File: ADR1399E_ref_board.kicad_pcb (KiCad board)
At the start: 4 copper layers, 119 x 60 mm, 103 parts, among them IC1 ADP7142ARDZ-R7, J1 Conn_01x02_Pin, J2 USB_C_Receptacle_PowerOnly_6P, J3 Conn_Coaxial, J4 S4B-XH-A, P1 JST_B2P_VH, Q1 MMBT3906, Q2 2N7002, U2 TPS61085DGK, U3 OPA182IDR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

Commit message: moved VH connector to center
avoid collision with Banana sockets (in case)
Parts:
- moved D2 26.3 mm to (138.4, 111.1), turned to -90 degrees
- moved P1 15.7 mm to (137.2, 104.0)
- moved R25 9.06 mm to (127.6, 104.2)
- moved R21 7.30 mm to (134.7, 109.6)
- moved TP8 6.22 mm to (143.5, 112.5)
- moved R18 5.10 mm to (131.4, 99.4), turned to -90 degrees
- moved C17 3.00 mm to (124.6, 94.9)
- moved C18 3.00 mm to (124.6, 92.6)
- moved TP7 2.69 mm to (143.5, 95.4)
- moved TP6 2.50 mm to (44.0, 128.0)
- moved U4 2.34 mm to (125.2, 99.0)
- moved RN1 1.10 mm to (122.0, 111.4)
- moved C23 0.90 mm to (122.1, 104.4)
- moved U7 0.89 mm to (121.9, 118.6)
- moved JP11 0.60 mm to (121.8, 125.8)
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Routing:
- net Net-(RN1-R1.2): track 16.3 -> 6.47 mm
- net /10V_Out: track 45.4 -> 40.1 mm
- net GND: track 42.0 -> 38.4 mm, vias 319 -> 324
- net Net-(U3-OUT): track 12.3 -> 9.95 mm
- net Net-(JP11-B): track 24.8 -> 26.7 mm
- net Net-(JP9-A): track 6.21 -> 7.31 mm
- net +BATT: track 96.1 -> 95.0 mm
- net Net-(Q1-B): track 36.9 -> 37.8 mm
- net Net-(RN1-R1.1): track 18.0 -> 17.2 mm
- net Net-(U4--IN): track 10.9 -> 10.3 mm
- net /15V_Out: track 42.2 -> 41.6 mm
- net Net-(JP8-A): track 4.98 -> 5.51 mm

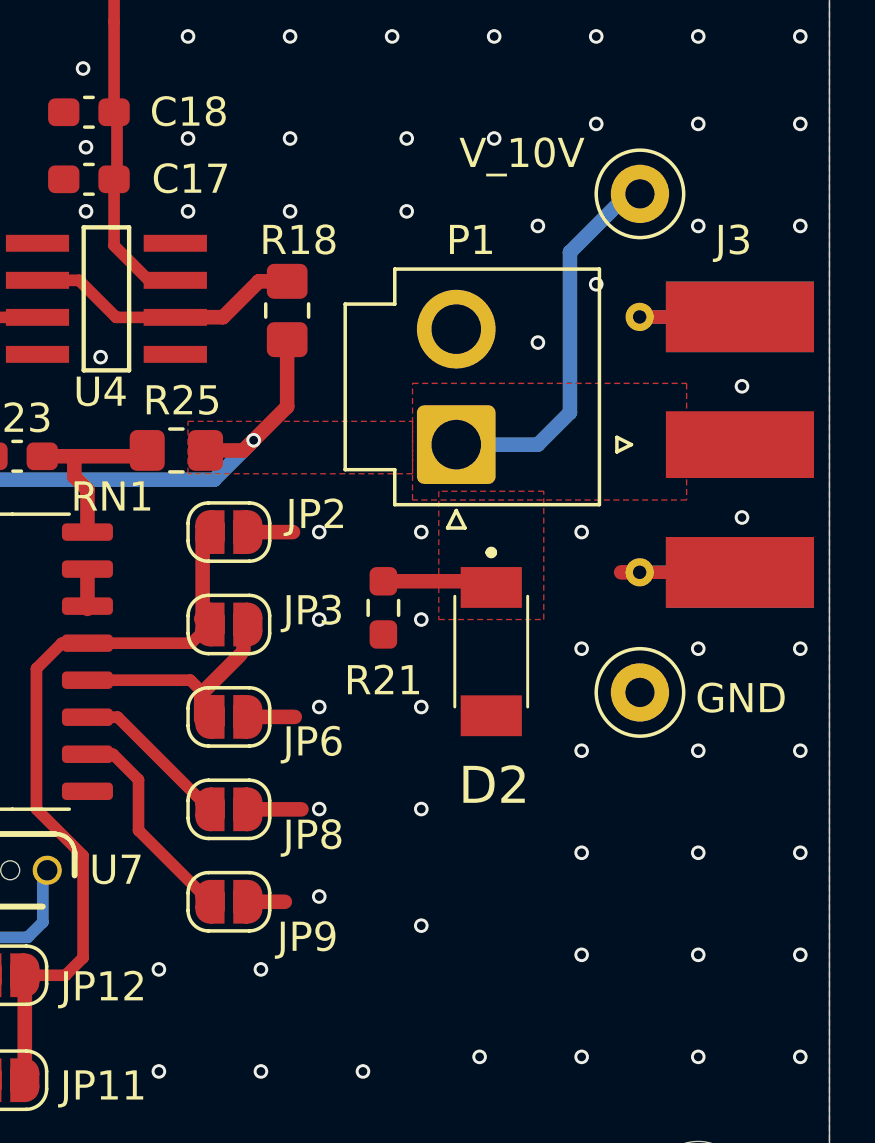
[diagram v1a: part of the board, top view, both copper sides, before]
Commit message: really centered the VH connector
And added VH housing 3d model
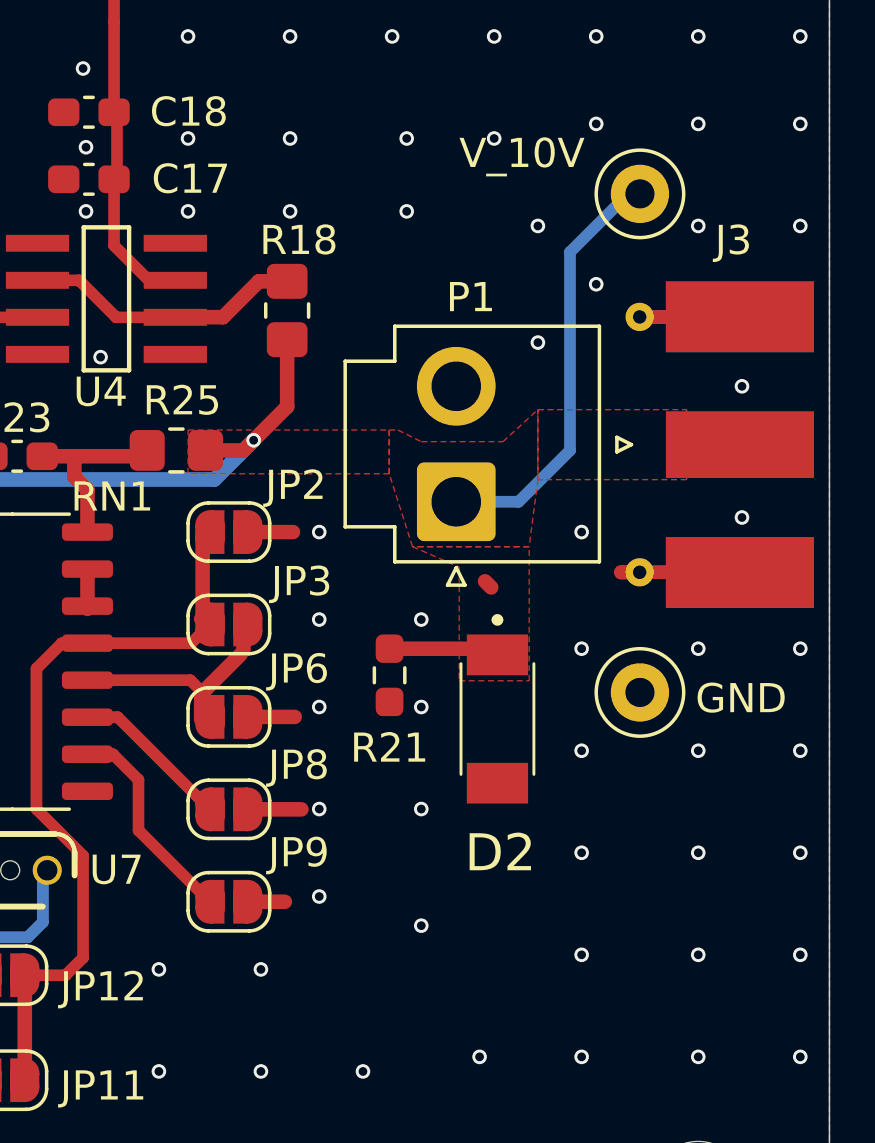
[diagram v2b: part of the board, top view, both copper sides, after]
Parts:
- moved D2 2.32 mm to (138.6, 113.4)
- moved R21 2.32 mm to (134.9, 111.9)
- moved P1 1.96 mm to (137.2, 106.0)
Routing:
- net /10V_Out: track 40.1 -> 41.7 mm
- net GND: vias 324 -> 323
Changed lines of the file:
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@@
 	(footprint "Resistor_SMD:R_0603_1608Metric_Pad0.98x0.95mm_HandSolder"
 		(layer "F.Cu")
-		(at 134.7 109.6 -90)
+		(at 134.9125 111.9125 -90)
 		(descr "Resistor SMD 0603 (1608 Metric), square (rectangular) end terminal, IPC-7351 nominal with elongated pad for handsoldering. (Body size source: IPC-SM-782 page 72, https://www.pcb-3d.com/wordpress/wp-content/uploads/ipc-sm-782a_amendment_1_and_2.pdf), generated with kicad-footprint-generator")
 		(tags "resistor handsolder")
@@
 		(tags "solder jumper open")
 		(property "Reference" "JP8"
-			(at 2.9 0.89 0)
+			(at 2.4 -1.51 0)
 			(layer "F.SilkS")
 			(effects
@@
 		(tags "solder jumper open")
 		(property "Reference" "JP9"
-			(at 2.7 1.22 0)
+			(at 2.4 -1.68 0)
 			(layer "F.SilkS")
 			(effects
@@
 		(tags "solder jumper open")
 		(property "Reference" "JP2"
-			(at 3 -0.6 0)
+			(at 2.3 -1.6 0)
 			(layer "F.SilkS")
 			(effects
@@
 	(footprint "Connector_JST:JST_VH_B2P-VH_1x02_P3.96mm_Vertical"
 		(layer "F.Cu")
-		(at 137.2 104 90)
+		(at 137.2 105.96 90)
 		(descr "JST VH series connector, B2P-VH (http://www.jst-mfg.com/product/pdf/eng/eVH.pdf), generated with kicad-footprint-generator")
 		(tags "connector JST VH vertical")
@@
 			)
 		)
+		(model "${KICAD_3RD_PARTY}/3dmodels/VHR-2N.STEP"
+			(offset
+				(xyz 2 0 17)
+			)
+			(scale
+				(xyz 1 1 1)
+			)
+			(rotate
+				(xyz 90 -0 -0)
+			)
+		)
 	)
 	(footprint "Capacitor_SMD:C_0603_1608Metric_Pad1.08x0.95mm_HandSolder"
@@
 		(tags "solder jumper open")
 		(property "Reference" "JP6"
-			(at 2.9 0.86 0)
+			(at 2.4 -1.64 0)
 			(layer "F.SilkS")
 			(effects
@@
 		(tags "solder jumper open")
 		(property "Reference" "JP3"
-			(at 2.9 -0.47 0)
+			(at 2.5 -1.47 0)
 			(layer "F.SilkS")
 			(effects
@@
 	(footprint "Samacsys:PMEG3050EP115"
 		(layer "F.Cu")
-		(at 138.4 111.1 -90)
+		(at 138.6125 113.4125 -90)
 		(descr "SOD128")
 		(tags "Diode ESD (Uni-directional)")
@@
 	)
 	(via
-		(at 136 107)
-		(size 0.5)
-		(drill 0.3)
-		(layers "F.Cu" "B.Cu")
-		(free yes)
-		(net 1)
-	)
-	(via
 		(at 93.1 98.4)
 		(size 0.5)
@@
 	)
 	(segment
-		(start 134.7 108.6875)
-		(end 138.1875 108.6875)
+		(start 134.9125 111)
+		(end 138.4 111)
 		(width 0.5)
 		(layer "F.Cu")
@@
 	)
 	(segment
-		(start 141.1 102.9)
-		(end 140 104)
+		(start 130.25 103.85)
+		(end 128.9 105.2)
 		(width 0.5)
 		(layer "B.Cu")
@@
 	)
 	(segment
-		(start 141.1 97.4)
-		(end 141.1 98)
-		(width 0.5)
+		(start 139.34 105.96)
+		(end 137.2 105.96)
+		(width 0.4)
 		(layer "B.Cu")
 		(net 20)
 	)
 	(segment
-		(start 130.25 103.85)
-		(end 128.9 105.2)
-		(width 0.5)
+		(start 141.1 97.4)
+		(end 141.1 104.2)
+		(width 0.4)
 		(layer "B.Cu")
 		(net 20)
 	)
 	(segment
-		(start 141.1 98)
-		(end 141.1 102.9)
-		(width 0.5)
+		(start 141.1 104.2)
+		(end 139.34 105.96)
+		(width 0.4)
 		(layer "B.Cu")
 		(net 20)
@@
 		(start 143.5 95)
 		(end 141.1 97.4)
-		(width 0.5)
-		(layer "B.Cu")
-		(net 20)
-	)
-	(segment
-		(start 140 104)
-		(end 137.2 104)
-		(width 0.5)
+		(width 0.4)
 		(layer "B.Cu")
 		(net 20)
@@
 		(polygon
 			(pts
-				(xy 128 103.2) (xy 135.7 103.2) (xy 135.7 105) (xy 128 105)
+				(xy 128 103.5) (xy 134.9 103.5) (xy 134.9 105) (xy 128 105)
 			)
 		)
@@
 		(polygon
 			(pts
-				(xy 145.1 101.9) (xy 145.1 105.9) (xy 135.7 105.9) (xy 135.7 101.9)
+				(xy 145.1 102.8) (xy 145.1 105.2) (xy 140 105.2) (xy 140 102.8)
 			)
 		)
@@
 	)
 	(zone
+		(net 20)
+		(net_name "/10V_Out")
+		(layer "F.Cu")
+		(hatch edge 0.5)
+		(priority 14)
+		(connect_pads yes
+			(clearance 0.2)
+		)
+		(min_thickness 0.25)
+		(filled_areas_thickness no)
+		(fill yes
+			(thermal_gap 0.5)
+			(thermal_bridge_width 0.5)
+		)
+		(polygon
+			(pts
+				(xy 134.9 103.5) (xy 135.2 103.5) (xy 136 103.9) (xy 138.8 103.9) (xy 140 102.8) (xy 140 105.2)
+				(xy 139.7 107.5) (xy 135.7 107.5) (xy 134.9 105)
+			)
+		)
+	)
+	(zone
 		(net 2)
 		(net_name "+5V")
@@
 		(polygon
 			(pts
-				(xy 136.6 110) (xy 140.2 110) (xy 140.2 105.6) (xy 136.6 105.6)
+				(xy 137.3 108.2) (xy 137.3 112.1) (xy 139.7 112.1) (xy 139.7 107.5) (xy 135.7 107.5)
 			)
 		)

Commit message: Update ADR1399E_ref_board.kicad_pcb
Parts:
- moved P1 0.14 mm to (137.2, 106.1)
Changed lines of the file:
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@@
 	(footprint "Connector_JST:JST_VH_B2P-VH_1x02_P3.96mm_Vertical"
 		(layer "F.Cu")
-		(at 137.2 105.96 90)
+		(at 137.2 106.1 90)
 		(descr "JST VH series connector, B2P-VH (http://www.jst-mfg.com/product/pdf/eng/eVH.pdf), generated with kicad-footprint-generator")
 		(tags "connector JST VH vertical")
@@
 			(pts
 				(xy 134.9 103.5) (xy 135.2 103.5) (xy 136 103.9) (xy 138.8 103.9) (xy 140 102.8) (xy 140 105.2)
-				(xy 139.7 107.5) (xy 135.7 107.5) (xy 134.9 105)
+				(xy 139.7 107.5) (xy 135.5 107.5) (xy 134.9 105)
 			)
 		)
@@
 		(polygon
 			(pts
-				(xy 137.3 108.2) (xy 137.3 112.1) (xy 139.7 112.1) (xy 139.7 107.5) (xy 135.7 107.5)
+				(xy 137.3 109.2) (xy 137.3 112.1) (xy 139.7 112.1) (xy 139.7 107.5) (xy 135.5 107.5)
 			)
 		)

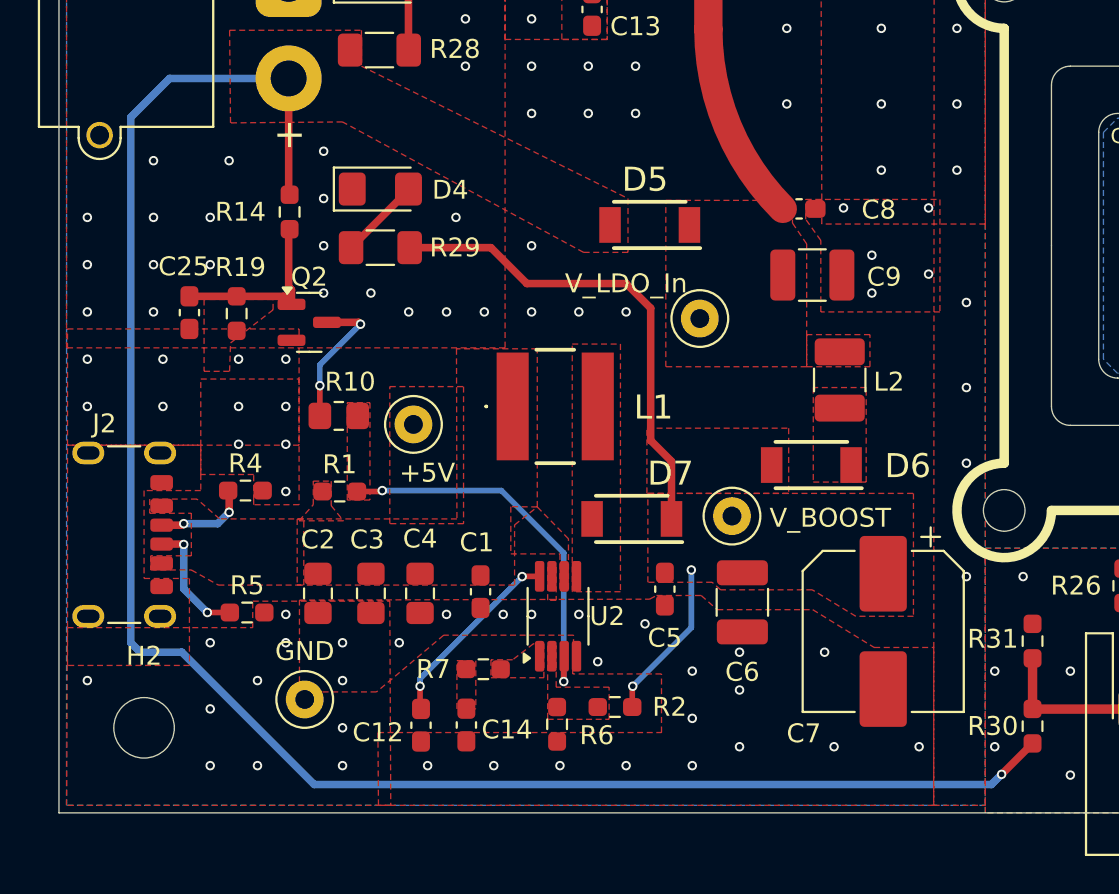
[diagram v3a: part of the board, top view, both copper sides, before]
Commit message: moved USB connector a bit
better enclosure fit
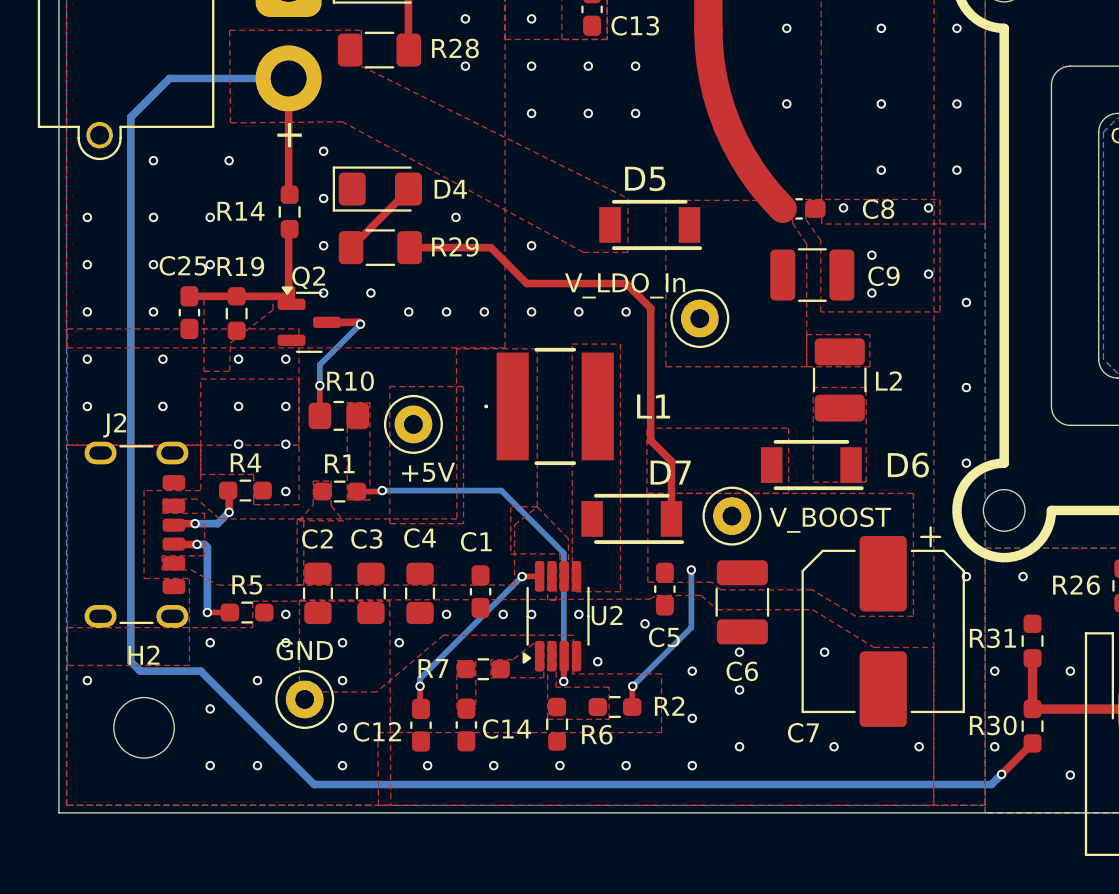
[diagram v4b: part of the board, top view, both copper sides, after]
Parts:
- moved J2 0.65 mm to (34.0, 119.3)
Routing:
- net Net-(J2-CC1): track 5.06 -> 4.41 mm
- net +BATT: track 95.0 -> 95.6 mm
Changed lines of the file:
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@@
 	(footprint "Connector_USB:USB_C_Receptacle_GCT_USB4125-xx-x-0190_6P_TopMnt_Horizontal"
 		(layer "F.Cu")
-		(at 33.35 119.28 -90)
+		(at 34 119.28 -90)
 		(descr "USB Type C Receptacle, GCT, power-only, 6P, top mounted, horizontal, 3A, 1.9mm stake: https://gct.co/files/drawings/usb4125.pdf")
 		(tags "USB C Type-C receptacle power-only charging-only 6P 6C right angled")
@@
 	)
 	(segment
-		(start 37.5 125.5)
-		(end 35.3 125.5)
+		(start 34.8 126)
+		(end 35.3 126.5)
 		(width 0.4)
 		(layer "B.Cu")
@@
 	)
 	(segment
-		(start 44.5 132.5)
-		(end 80 132.5)
-		(width 0.4)
-		(layer "B.Cu")
-		(net 17)
-	)
-	(segment
-		(start 36.85 95.15)
-		(end 34.8 97.2)
+		(start 35.3 126.5)
+		(end 38.5 126.5)
 		(width 0.4)
 		(layer "B.Cu")
@@
 	)
 	(segment
-		(start 43.15 95.15)
-		(end 36.85 95.15)
+		(start 34.8 97.2)
+		(end 34.8 126)
 		(width 0.4)
 		(layer "B.Cu")
@@
 	(segment
 		(start 80.325 132.5)
-		(end 80 132.5)
+		(end 80.8625 131.9625)
 		(width 0.4)
 		(layer "B.Cu")
@@
 	)
 	(segment
-		(start 35.3 125.5)
-		(end 34.8 125)
+		(start 38.5 126.5)
+		(end 44.5 132.5)
 		(width 0.4)
 		(layer "B.Cu")
@@
 	)
 	(segment
-		(start 80.8625 131.9625)
+		(start 44.5 132.5)
 		(end 80.325 132.5)
 		(width 0.4)
@@
 	)
 	(segment
-		(start 34.8 97.2)
-		(end 34.8 125)
+		(start 43.15 95.15)
+		(end 36.85 95.15)
 		(width 0.4)
 		(layer "B.Cu")
@@
 	)
 	(segment
-		(start 44.5 132.5)
-		(end 37.5 125.5)
+		(start 36.85 95.15)
+		(end 34.8 97.2)
 		(width 0.4)
 		(layer "B.Cu")
@@
 	)
 	(segment
-		(start 36.43 119.78)
-		(end 37.58 119.78)
+		(start 37.1 119.8)
+		(end 37.08 119.78)
 		(width 0.4)
 		(layer "F.Cu")
@@
 	)
 	(segment
-		(start 37.58 119.78)
-		(end 37.6 119.8)
+		(start 38.3 119.8)
+		(end 37.1 119.8)
 		(width 0.4)
 		(layer "F.Cu")
@@
 	)
 	(via
-		(at 38.85 123.4)
+		(at 38.3 119.8)
 		(size 0.5)
 		(drill 0.3)
@@
 	)
 	(via
-		(at 37.6 119.8)
+		(at 38.85 123.4)
 		(size 0.5)
 		(drill 0.3)
@@
 	)
 	(segment
-		(start 37.6 119.8)
-		(end 37.6 122.15)
+		(start 38.85 123.4)
+		(end 38.85 119.95)
 		(width 0.4)
 		(layer "B.Cu")
@@
 	)
 	(segment
-		(start 37.6 122.15)
-		(end 38.85 123.4)
+		(start 38.85 119.95)
+		(end 38.7 119.8)
 		(width 0.4)
 		(layer "B.Cu")
@@
 	)
 	(segment
-		(start 40 117)
-		(end 39.95 116.95)
+		(start 38.7 119.8)
+		(end 38.3 119.8)
+		(width 0.4)
+		(layer "B.Cu")
+		(net 18)
+	)
+	(segment
+		(start 37.16 118.7)
+		(end 37.08 118.78)
 		(width 0.4)
 		(layer "F.Cu")
@@
 	)
 	(segment
-		(start 40 118.1)
-		(end 40 117)
+		(start 38.2 118.7)
+		(end 37.16 118.7)
 		(width 0.4)
 		(layer "F.Cu")
@@
 	)
 	(segment
-		(start 40 116.975)
-		(end 40.025 116.95)
-		(width 0.3)
+		(start 40 117)
+		(end 39.95 116.95)
+		(width 0.4)
 		(layer "F.Cu")
 		(net 19)
 	)
 	(segment
-		(start 36.43 118.78)
-		(end 37.52 118.78)
+		(start 40 118.1)
+		(end 40 117)
 		(width 0.4)
 		(layer "F.Cu")
@@
 	)
 	(segment
-		(start 37.52 118.78)
-		(end 37.6 118.7)
-		(width 0.4)
+		(start 40 116.975)
+		(end 40.025 116.95)
+		(width 0.3)
 		(layer "F.Cu")
 		(net 19)
@@
 	)
 	(via
-		(at 37.6 118.7)
+		(at 38.2 118.7)
 		(size 0.5)
 		(drill 0.3)
@@
 	(segment
 		(start 39.4 118.7)
-		(end 40 118.1)
+		(end 38.2 118.7)
 		(width 0.4)
 		(layer "B.Cu")
@@
 	)
 	(segment
-		(start 37.6 118.7)
-		(end 39.4 118.7)
+		(start 39.4 118.7)
+		(end 40 118.1)
 		(width 0.4)
 		(layer "B.Cu")
@@
 		(polygon
 			(pts
-				(xy 35.85 120.4) (xy 35.85 121.15) (xy 38 121.15) (xy 39.431797 121.95) (xy 43.95 121.95) (xy 43.95 118.45)
-				(xy 39.5 118.45) (xy 38.3 117.4) (xy 35.8 117.4) (xy 35.8 118.15) (xy 38 118.15) (xy 38 120.4)
+				(xy 36.45 120.4) (xy 36.45 121.15) (xy 38 121.15) (xy 39.431797 121.95) (xy 43.95 121.95) (xy 43.95 118.45)
+				(xy 39.5 118.45) (xy 38.3 117.4) (xy 36.5 117.4) (xy 36.5 118.15) (xy 38.7 118.15) (xy 38.7 120.4)
 			)
 		)
